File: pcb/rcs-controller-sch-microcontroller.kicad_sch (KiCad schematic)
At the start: 21 parts, among them J4 Screw_Terminal_4_P3.50mm, Q2 SI7465DP-T1-E3, Q3 SI7465DP-T1-E3, Q4 PMV45EN2, Q5 PMV45EN2, U1 LSM6DSOX, U4 FeatherS3

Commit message: Submit for review 4.23.2025
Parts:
- removed D6, D8: LED, LED_SMD:LED_0603_1608Metric, symbol Device:LED
- added LED1, LED2: LED_0603_Amber, PCM_LED_SMD_AKL:LED_0603_1608Metric, symbol PCM_LED_AKL:LED_0603_Amber
- added R26, R27: 10k, Resistor_SMD:R_0603_1608Metric, symbol Device:R_Small_US
- added TP33, TP34: Test-Point, psas-footprints:TP-through-hole-1X01, symbol psas-testpoint:Test-Point
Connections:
- net +3.3V: now also R26.1, R27.1
- net GND: now also LED1.2 (A), LED2.2 (A)
- net at R25.2: now also LED1.1 (K)
- net at U1.13 (SCL), U4.19 (IO5): now also R27.2, TP34.1
- net at U1.14 (SDA), U4.20 (IO6): now also R26.2, TP33.1
- net at R24.2: now also LED2.1 (K)
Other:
- note added: "6 DOF IMU"
- note added: "Clockwise"
- note added: "Counter-Clockwise"
- moved on the sheet: C19, C20, U1

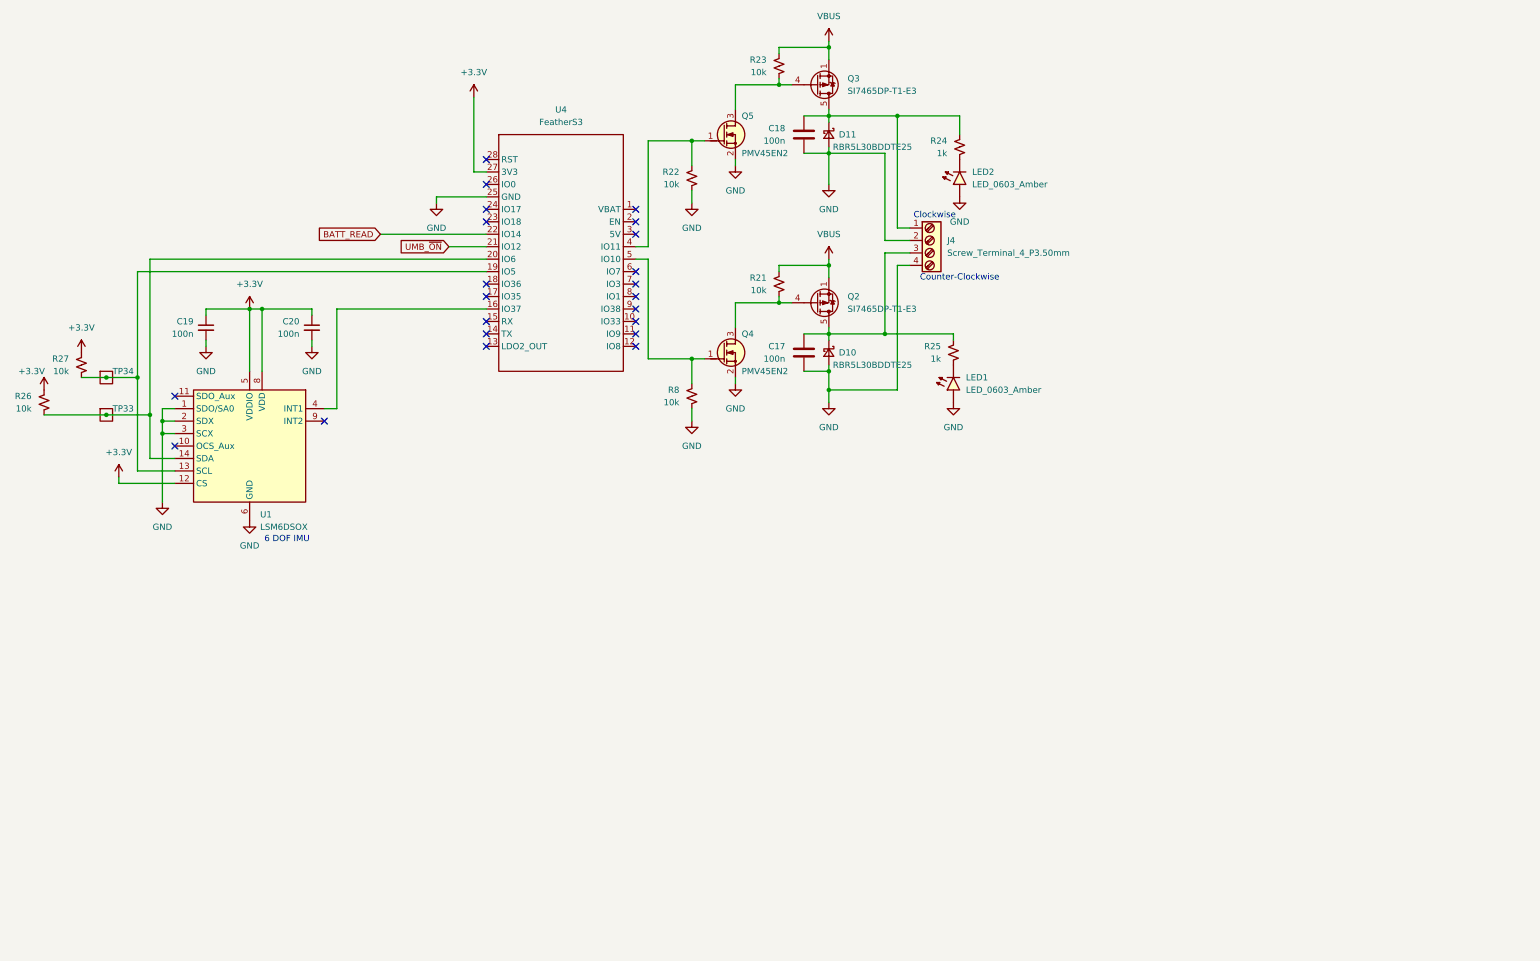
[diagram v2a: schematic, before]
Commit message: Fixed BOM, fixed missing symbol and footprint libraries, stitched vias, generated Gerbers.
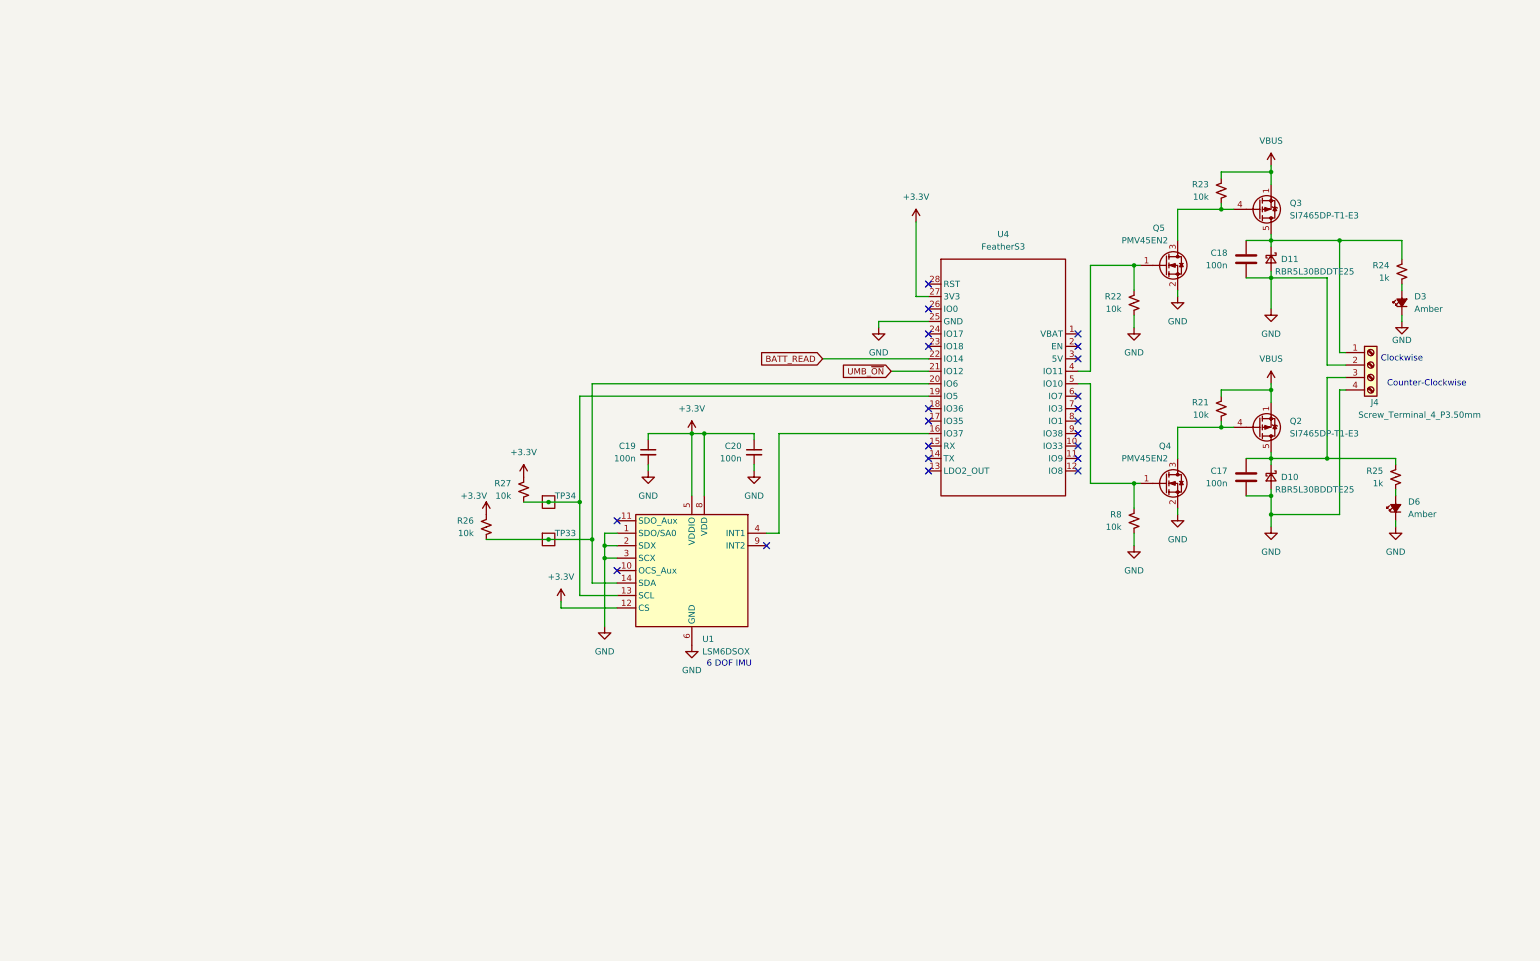
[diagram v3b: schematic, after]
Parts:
- D3: renamed from LED2; value LED_0603_Amber -> Amber; footprint PCM_LED_SMD_AKL:LED_0603_1608Metric -> LED_SMD:LED_0603_1608Metric; symbol PCM_LED_AKL:LED_0603_Amber -> Device:LED_Small_Filled; DPN (none) -> 732-4981-1-ND; DST (none) -> DigiKey; MFR (none) -> Wurth; MPN (none) -> 150060YS75000
- D6: renamed from LED1; value LED_0603_Amber -> Amber; footprint PCM_LED_SMD_AKL:LED_0603_1608Metric -> LED_SMD:LED_0603_1608Metric; symbol PCM_LED_AKL:LED_0603_Amber -> Device:LED_Small_Filled; DPN (none) -> 732-4981-1-ND; DST (none) -> DigiKey; MFR (none) -> Wurth; MPN (none) -> 150060YS75000
- J4: symbol PCM_SL_Screw_Terminal:Screw_Terminal_4_P3.50mm -> Connector:Screw_Terminal_01x04; DPN (none) -> 277-5744-ND; DST (none) -> DigiKey; MFR (none) -> Phoenix Contact; MPN (none) -> 1751264
- Q2, Q3: footprint PCM_Package_SON_AKL:Infineon_PG-TDSON-8 -> Package_SO:PowerPAK_SO-8_Single
- Q4, Q5: footprint PCM_Package_TO_SOT_SMD_AKL:SOT-23 -> Package_TO_SOT_SMD:SOT-23-3; symbol PCM_Transistor_MOSFET_AKL:PMV45EN2 -> Transistor_FET:Q_NMOS_GSD; DPN (none) -> 1727-2307-1-ND; DST (none) -> DigiKey; MFR (none) -> Nexperia USA Inc.; MPN (none) -> PMV45EN2R
- U1: DPN (none) -> 497-18367-1-ND; DST (none) -> DigiKey; MFR (none) -> STMicroelectronics; MPN (none) -> LSM6DSOXTR
- U4: symbol Additional_symbols:FeatherS3 -> psas-ics:FeatherS3; DPN (none) -> 5477; DST (none) -> AdaFruit; MFR (none) -> AdaFruit; MPN (none) -> ESP32-S3 Feather
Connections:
- net GND: now also D3.1 (K), D6.1 (K); no longer D3.2 (A), D6.2 (A)
- net at R25.2: now also D6.2 (A); no longer D6.1 (K)
- net at R24.2: now also D3.2 (A); no longer D3.1 (K)
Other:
- moved on the sheet: C17, C18, C19, C20, D10, D11, J4, Q2, Q3, R21, R22, R23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

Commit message: Rev 2.0
Updated board with ESP32 chip to replace feather
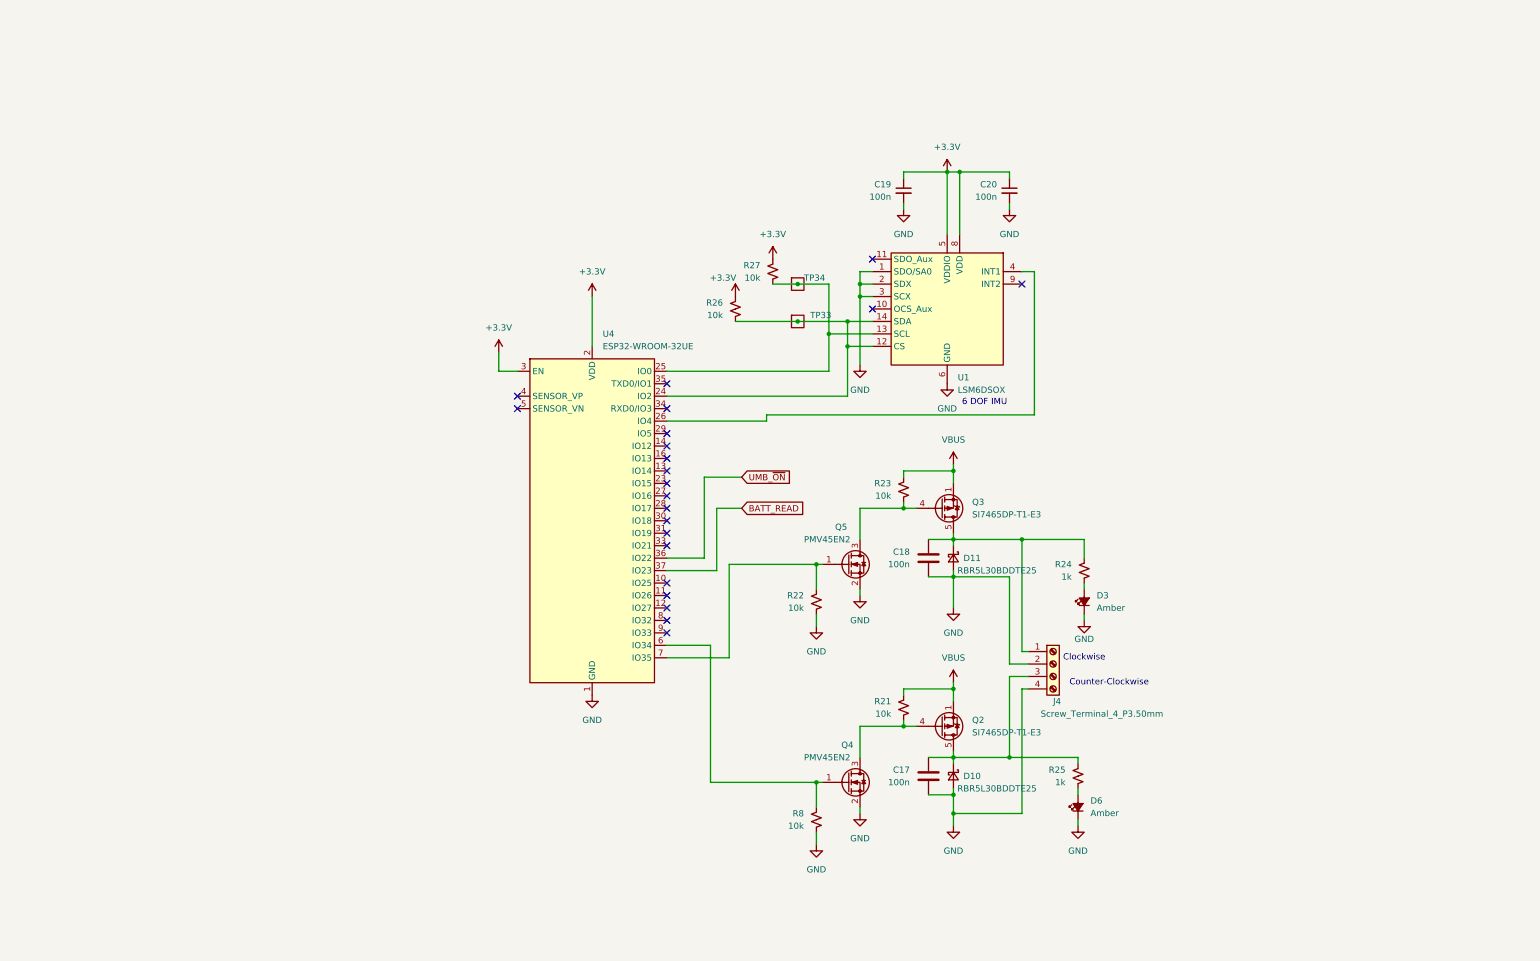
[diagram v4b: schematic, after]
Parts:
- removed U4: FeatherS3, Module:Adafruit_Feather, symbol psas-ics:FeatherS3
- added U4: ESP32-WROOM-32UE, RF_Module:ESP32-WROOM-32UE, symbol RF_Module:ESP32-WROOM-32UE
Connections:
- net +3.3V: now also U4.2 (VDD), U4.3 (EN); no longer U1.12 (CS)
- net BATT_READ: now also U4.37 (IO23)
- net GND: now also U4.1 (GND), U4.15 (GND), U4.38 (GND), U4.39 (GND)
- net UMB_~{ON}: now also U4.36 (IO22)
- net at Q5.1 (G), R22.1: now also U4.7 (IO35)
- net at Q4.1 (G), R8.1: now also U4.6 (IO34)
- net at R26.2, TP33.1, U1.14 (SDA): now also U1.12 (CS), U4.24 (IO2)
- net at R27.2, TP34.1, U1.13 (SCL): now also U4.25 (IO0)
- net at U1.4 (INT1): now also U4.26 (IO4)
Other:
- moved on the sheet: C17, C18, C19, C20, D10, D11, D3, D6, J4, Q2, Q3, Q4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

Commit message: Revision 6/2
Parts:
- removed U4: ESP32-WROOM-32UE, RF_Module:ESP32-WROOM-32UE, symbol RF_Module:ESP32-WROOM-32UE
- added C21, C22: 1p, Capacitor_SMD:C_0603_1608Metric, symbol Device:C
- added J5: USB_C_Receptacle_USB2.0_14P, symbol Connector:USB_C_Receptacle_USB2.0_14P
- added J6: Conn_01x03, symbol Connector_Generic:Conn_01x03
- added R28, R29: 5k, Resistor_SMD:R_0603_1608Metric, symbol Device:R_Small_US
- added R30: 10k, Resistor_SMD:R_0603_1608Metric, symbol Device:R_Small_US
- added SW?: SW_Push, symbol Switch:SW_Push
- added U4: ESP32-S3-WROOM-1, RF_Module:ESP32-S3-WROOM-1, symbol RF_Module:ESP32-S3-WROOM-1
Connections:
- net +3.3V: now also R30.1, SW?.1, U4.2 (3V3)
- net BATT_READ: now also U4.17 (IO9)
- net GND: now also C21.2, C22.2, J5.A1 (GND), J5.A12 (GND), J5.B1 (GND), J5.B12 (GND), J6.3 (Pin_3), R28.2, R29.2, SW?.2, U4.1 (GND), U4.40 (GND), U4.41 (GND)
- net UMB_~{ON}: now also U4.12 (IO8)
- net at Q5.1 (G), R22.1: now also U4.9 (IO16)
- net at Q4.1 (G), R8.1: now also U4.8 (IO15)
- net at R26.2, TP33.1, U1.12 (CS)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: now also U4.15 (IO3)
- net at R27.2, TP34.1, U1.13 (SCL): now also U4.38 (IO2)
- net at U1.4 (INT1): now also U4.4 (IO4)
- new net: J5.A5 (CC1), R29.1
- new net: C22.1, R30.2, U4.3 (EN)
- new net: C21.1, J5.S1 (SHIELD)
- new net: J6.1 (Pin_1), U4.36 (RXD0)
- new net: J6.2 (Pin_2), U4.37 (TXD0)
- new net: J5.A7 (D-), J5.B7 (D-), U4.13 (USB_D-)
- new net: J5.A6 (D+), J5.B6 (D+), U4.14 (USB_D+)
- new net: J5.A4 (VBUS), J5.A9 (VBUS), J5.B4 (VBUS), J5.B9 (VBUS)
- new net: J5.B5 (CC2), R28.1
- no-connect marks 22 -> 29
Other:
- moved on the sheet: C17, C18, D10, D11, D3, D6, J4, Q2, Q3, Q4, Q5, R21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

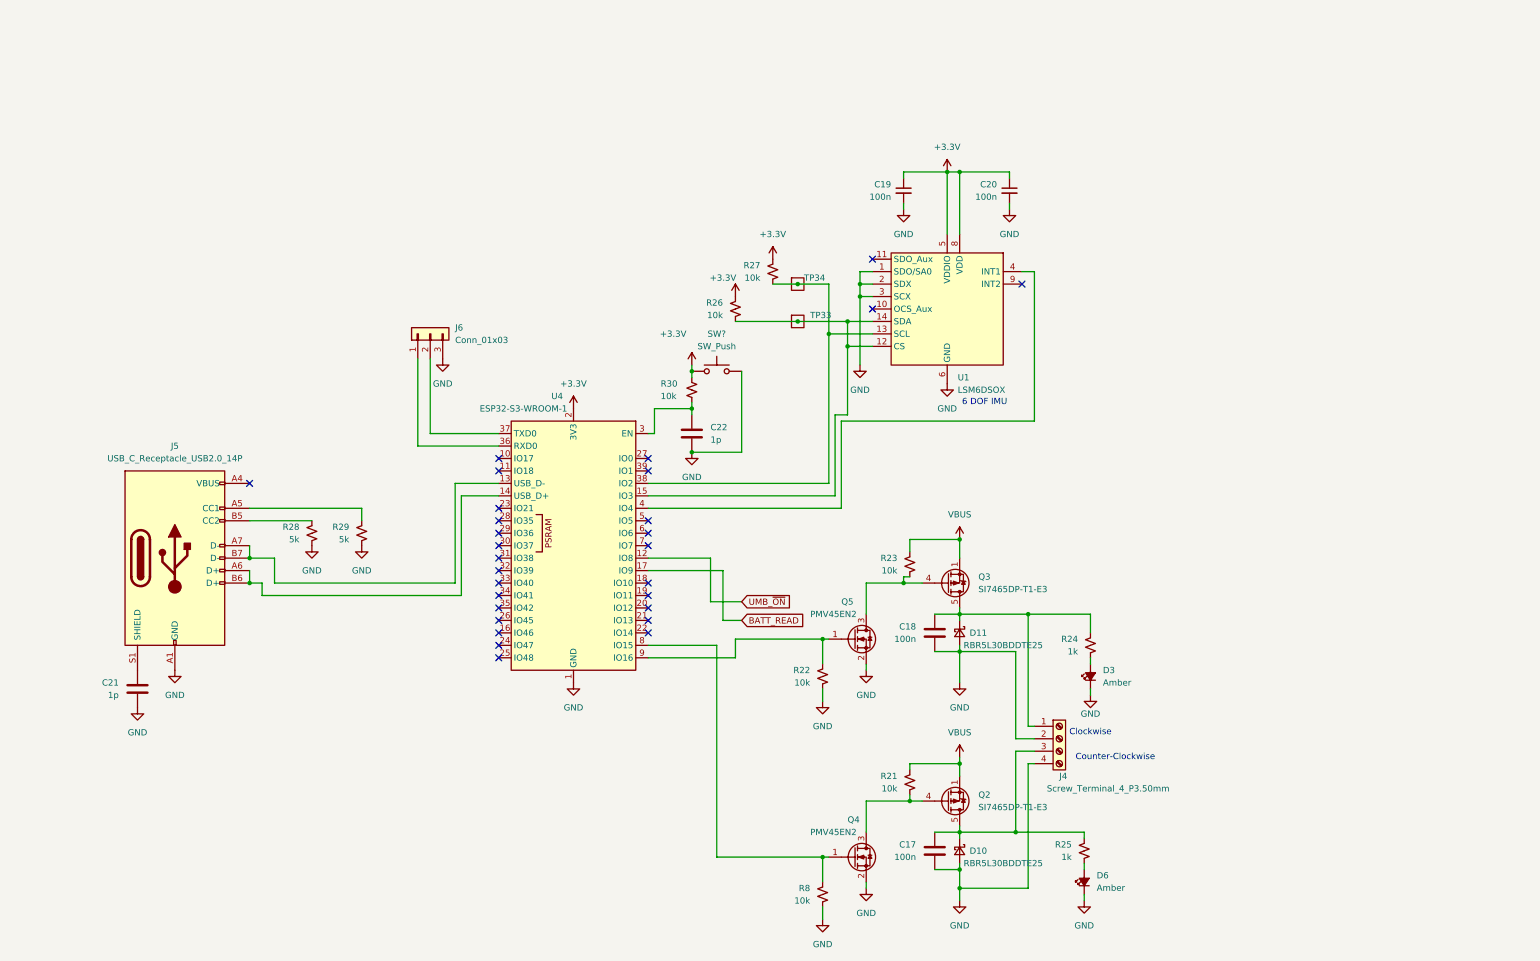
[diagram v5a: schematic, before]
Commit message: Design review; fix schematic issues and some polish, some board to schematic patching, fix footprint issues.
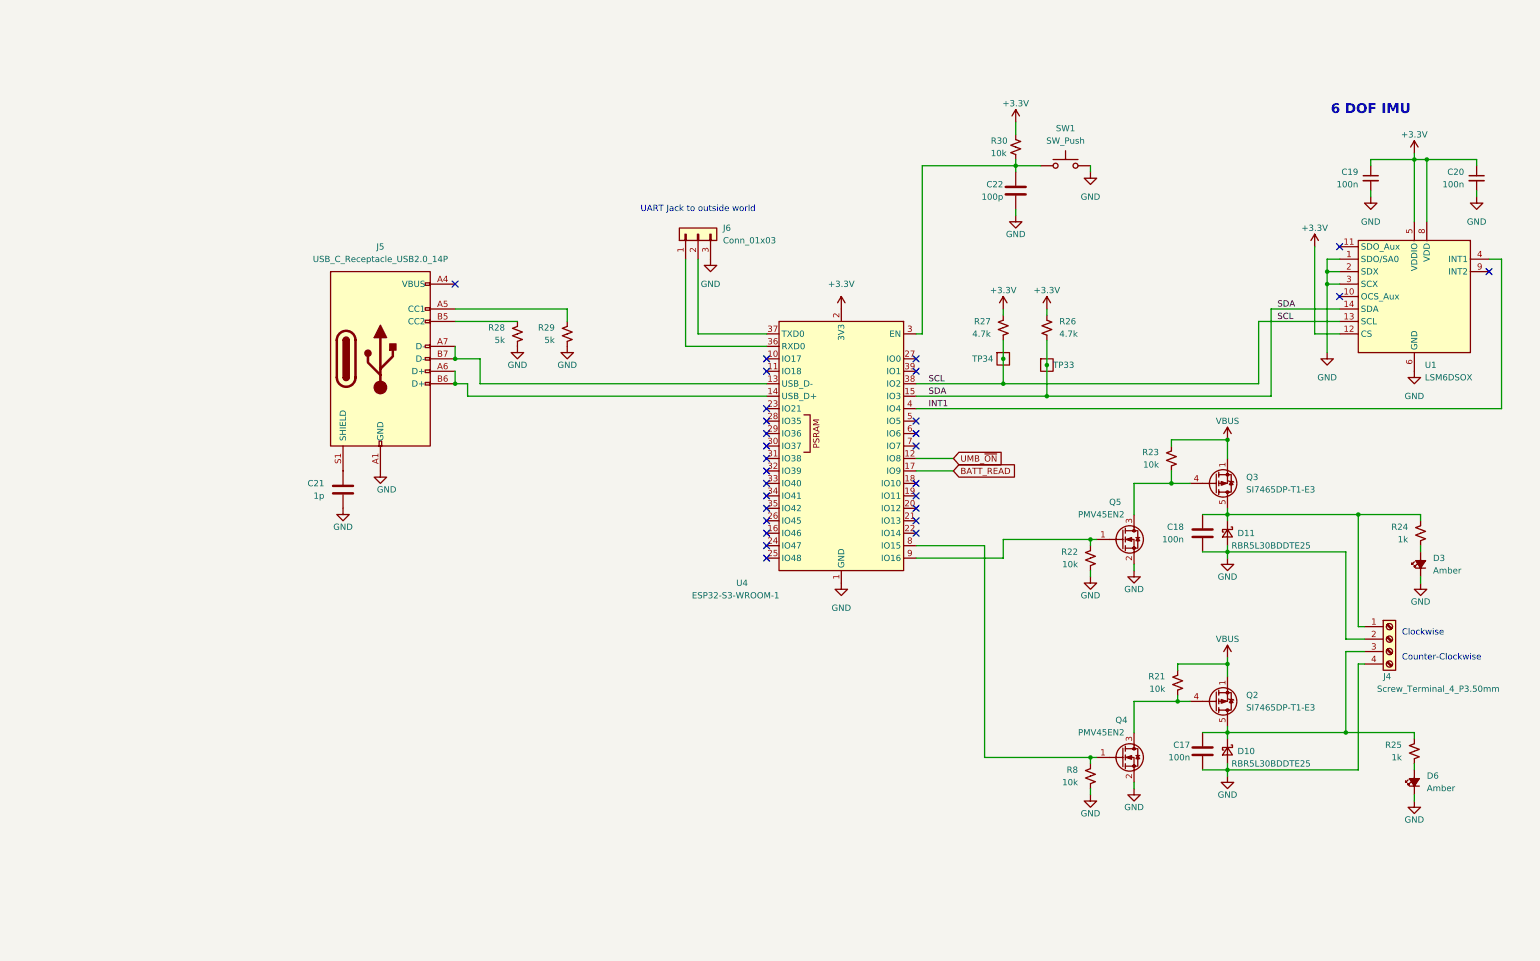
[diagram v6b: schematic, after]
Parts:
- C22: value 1p -> 100p
- J5: footprint (none) -> Connector_USB:USB_C_Receptacle_Palconn_UTC16-G
- J6: footprint (none) -> Connector_PinHeader_2.54mm:PinHeader_1x03_P2.54mm_Vertical
- R26, R27: value 10k -> 4.7k
- SW1: renamed from SW?; footprint (none) -> Button_Switch_THT:SW_PUSH_6mm
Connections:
- net +3.3V: now also U1.12 (CS); no longer SW1.1
- net at C22.1, R30.2, U4.3 (EN): now also SW1.1
- net SDA: now reaches R26.2, TP33.1, U1.14 (SDA), U4.15 (IO3)
- net SDA: no longer U1.12 (CS)
- net SCL: now reaches R27.2, TP34.1, U1.13 (SCL), U4.38 (IO2)
- net INT1: now reaches U1.4 (INT1), U4.4 (IO4)
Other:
- note added: "UART Jack to outside world"
- moved on the sheet: C17, C18, C19, C20, C21, C22, D10, D11, D3, D6, J4, J5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

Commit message: Push for design review 6.24
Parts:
- J5: DPN (none) -> 2073-USB4105-GF-ACT-ND; DST (none) -> Digikey; MFR (none) -> GCT; MPN (none) -> USB4105-GF-A
- R21, R22, R23, R30, R8: DPN (none) -> 311-10.0KHRCT-ND; DST (none) -> DigiKey
- R24, R25: DPN (none) -> 311-1.00KHRCT-ND; DST (none) -> DigiKey
- R26, R27: DPN (none) -> 311-4.70KHRCT-ND; DST (none) -> DigiKey; MPN RC0603FR-0710KL -> RC0603FR-074K7L
- R28, R29: DPN (none) -> 311-4.70KHRCT-ND; DST (none) -> DigiKey
- SW1: DPN (none) -> SW400-ND; MFR (none) -> Omron Electronics Inc-EMC Div; MPN (none) -> B3F-1000
- U4: DPN (none) -> 5407-ESP32-S3-WROOM-1-N4R8CT-ND; DST (none) -> Digikey; MFR (none) -> Espressif Systems; MPN (none) -> ESP32-S3-WROOM-1-N4R8
